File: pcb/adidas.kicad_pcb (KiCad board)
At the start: 2 copper layers, 152.7 x 107.2 mm, 34 parts, among them J1 ISP Header, J2 Shitty Add-on, J4 Battery, U1 MPU-6050, U2 ATTINY841-SSU

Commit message: RUN DRC
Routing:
- net GND: track 0.00 -> 367.1 mm, vias 0 -> 2
- net /7(SDA): track 0.00 -> 189.3 mm
- net /4(RST): track 0.00 -> 169.9 mm
- net /9(SCL): track 0.00 -> 167.8 mm, vias 0 -> 2
- net VCC: track 0.00 -> 149.7 mm
- net /3(LED Mid Row): track 0.00 -> 127.5 mm
- net Net-(D8-Pad2): track 0.00 -> 124.8 mm, vias 0 -> 1
- net Net-(J1-Pin_1): track 0.00 -> 121.6 mm, vias 0 -> 1
- net /2(LED Bottom Row): track 0.00 -> 101.6 mm
- net Net-(D4-Pad2): track 0.00 -> 100.2 mm, vias 0 -> 1
- net /13(SAO1): track 0.00 -> 92.9 mm, vias 0 -> 1
- net /12(SAO2): track 0.00 -> 90.5 mm, vias 0 -> 2
- net /5(LED Top Row): track 0.00 -> 88.3 mm, vias 0 -> 2
- net Net-(D1-Pad2): track 0.00 -> 71.6 mm, vias 0 -> 1
- net +BATT: track 0.00 -> 59.2 mm
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
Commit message: cleanup for v0.2
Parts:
- J4: value Battery -> мощность
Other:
- board text added: "THE @DEAD10C5 LOVE YOU!! @p0lr_ - Eddie the Yeti yaya_pancho - @thedevilsvoice"
- board text removed: "THE @DEAD10C5 LOVE YOU!! @p0lr_ - Eddie the Yeti yaya_pancho - @5l0w0n3 @thedevilsvoice"
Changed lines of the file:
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@@
         (effects (font (size 1 1) (thickness 0.15)) (justify mirror))
     )
-    (fp_text value "Battery" (at 0 -5.31) (layer "B.Fab")
+    (fp_text value "мощность" (at 0 -5.31) (layer "B.Fab")
         (effects (font (size 1 1) (thickness 0.15)) (justify mirror))
     )
@@
   (gr_line (start 100.93 110.14) (end 101.36 110.81)
     (stroke (width 0.1) (type solid)) (layer "Edge.Cuts"))
+  (gr_text "-" (at 150.9014 137.541) (layer "B.SilkS")
+    (effects (font (size 1.5 1.5) (thickness 0.3) bold) (justify left bottom mirror))
+  )
   (gr_text "SCK" (at 117.3226 100.0252 90) (layer "B.SilkS")
     (effects (font (size 0.8 0.8) (thickness 0.15)) (justify mirror))
@@
     (effects (font (size 0.6 0.6) (thickness 0.15)) (justify mirror))
   )
-  (gr_text "-" (at 106.7816 86.6394 180) (layer "B.SilkS")
-    (effects (font (size 0.6 0.6) (thickness 0.15)) (justify mirror))
-  )
   (gr_text "взаимоблокировщики - 31 октябрь 2022 г." (at 164.846 111.2012) (layer "B.SilkS")
     (effects (font (size 2 2) (thickness 0.3)) (justify mirror))
@@
     (effects (font (size 0.6 0.6) (thickness 0.15)) (justify mirror))
   )
-  (gr_text "THE @DEAD10C5 LOVE YOU!!\n@p0lr_ - Eddie the Yeti\nyaya_pancho - @5l0w0n3\n@thedevilsvoice " (at 228.6508 78.4352) (layer "B.SilkS")
+  (gr_text "THE @DEAD10C5 LOVE YOU!!\n@p0lr_ - Eddie the Yeti\nyaya_pancho - @thedevilsvoice " (at 228.6508 78.4352) (layer "B.SilkS")
     (effects (font (size 0.3 0.3) (thickness 0.075)) (justify mirror))
   )
@@
     (effects (font (size 2 2) (thickness 0.15)) (justify mirror))
   )
-  (gr_text "+" (at 101.4476 86.614 90) (layer "B.SilkS")
-    (effects (font (size 0.6 0.6) (thickness 0.15)) (justify mirror))
-  )
   (gr_text "Русский хардбасс" (at 165.1 123.0376) (layer "B.SilkS")
     (effects (font (size 3 3) (thickness 0.5)) (justify mirror))
@@
     (effects (font (size 0.8 0.8) (thickness 0.15)) (justify mirror))
   )
+  (gr_text "+" (at 150.9522 134.493) (layer "B.SilkS")
+    (effects (font (size 1.5 1.5) (thickness 0.3) bold) (justify left bottom mirror))
+  )
   (dimension (type aligned) (layer "B.Cu")

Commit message: final v0.2
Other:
- board text added: "SCL"
- board text added: "SDA"
- board text removed: "MISO"
- board text removed: "MOSI"
- board text removed: "SCK"

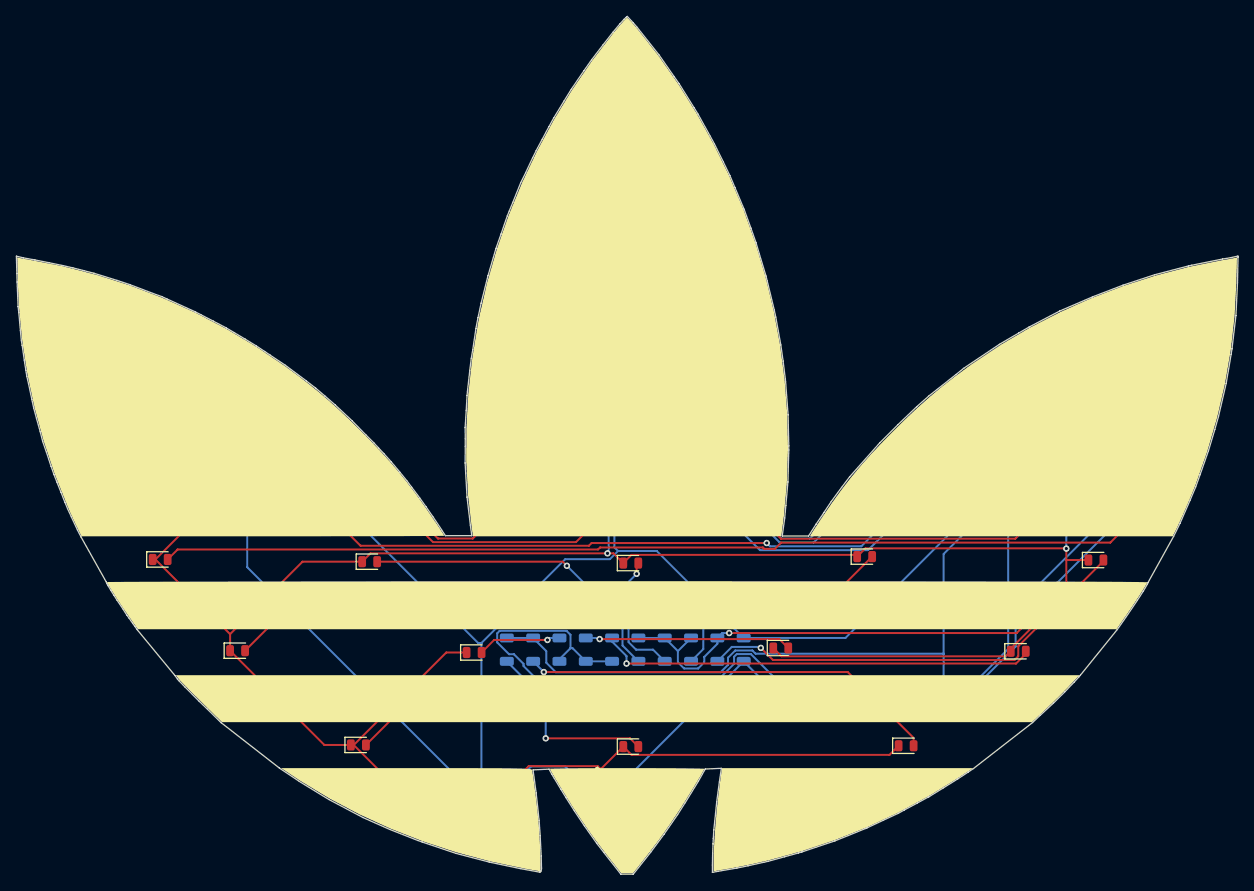
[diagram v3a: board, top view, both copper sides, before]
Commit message: make some changes from PCBway feedback v0.3 (#27)
* make some changes from PCBway feedback v0.3

* tune actions

* add mouser and digikey part numbers

* run ERC checks

* run ERC checks
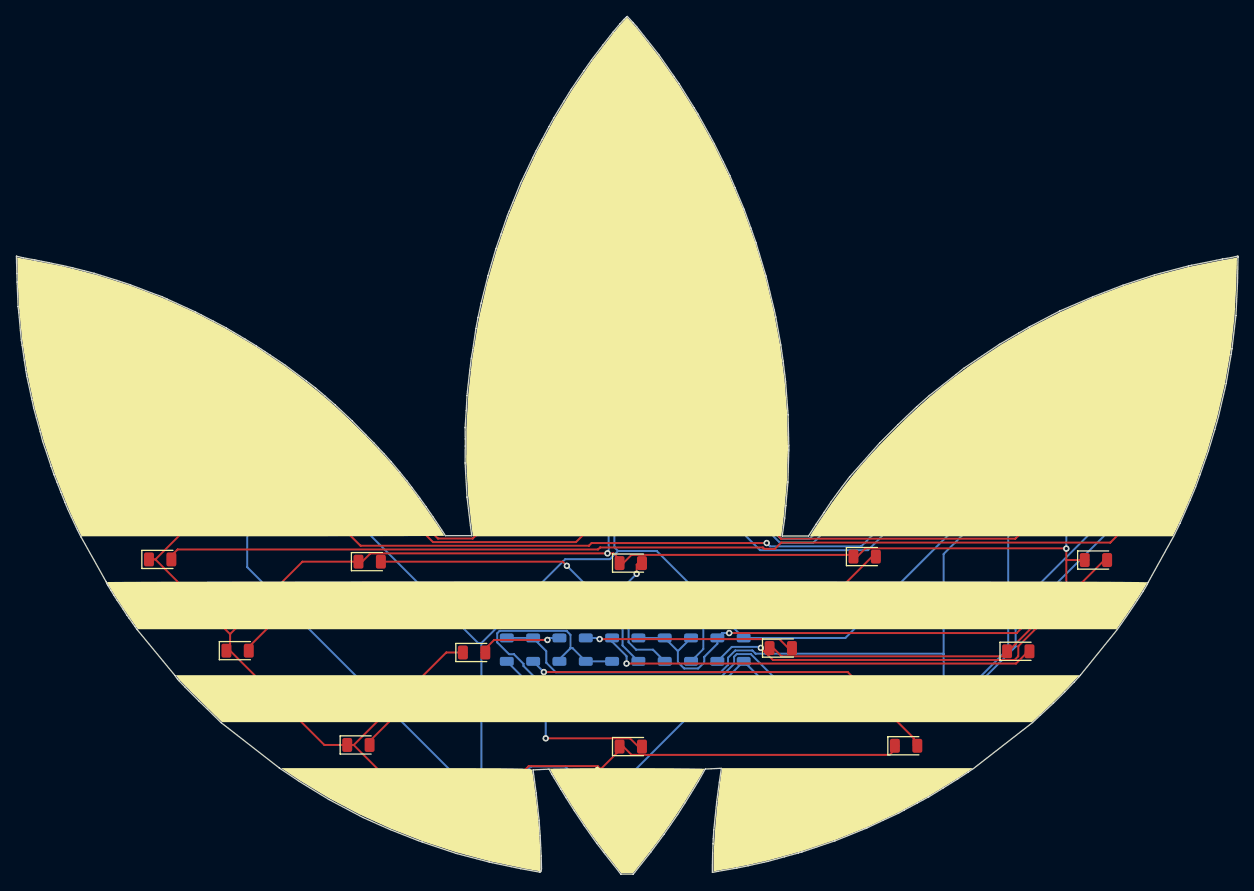
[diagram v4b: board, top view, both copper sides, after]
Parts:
- removed BT1: Battery_Cell, Battery:BatteryHolder_Keystone_3002_1x2032
- removed REF**: MountingHole_4.5mm, MountingHole:MountingHole_4.5mm
- D1, D10, D12, D2, D3, D4, D5, D6, D7, D8, D9: value LHN974 -> AP3216SYCK; footprint LED_SMD:LED_0805_2012Metric -> LED_SMD:LED_1206_3216Metric
- D11: value ~ -> AP3216SYCK; footprint LED_SMD:LED_0805_2012Metric -> LED_SMD:LED_1206_3216Metric
- J4: value мощность -> Battery
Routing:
- net +BATT: track 59.2 -> 0.00 mm
- net (no net): track 0.00 -> 59.2 mm

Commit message: BOM updates (#29)
* update schematic

* update schematic

* update the battery clip in the BOM
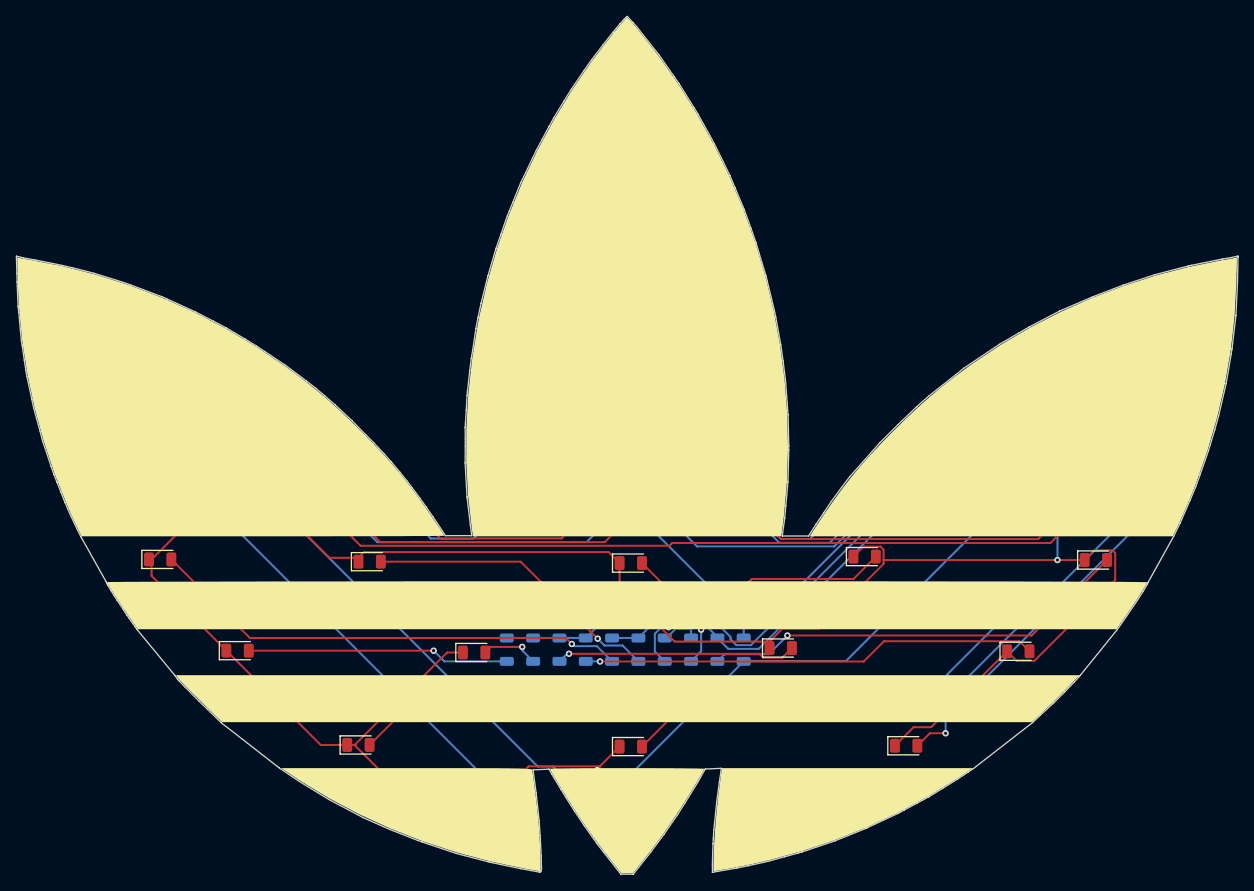
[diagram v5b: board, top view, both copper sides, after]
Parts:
- added BT1: Battery Clip, DEAD10C5:BatteryHolder_Keystone_3002_1x2032, B.Cu at (165.4, 82.8)
- D1, D10, D11, D12, D2, D3, D4, D5, D6, D7, D8, D9: value AP3216SYCK -> CTL1206FWH1T
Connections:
- J1 pad 2: VCC -> VDD
- J2 pad 1: VCC +3.3V -> VDD
- J4 pad 1: VCC -> VDD
- R13 pad 1: VCC -> VDD
- R2 pad 1: Net-(D4-Pad2) -> /2(LED Bottom Row)
- R2 pad 2: /3(LED Mid Row) -> Net-(D2-Pad2)
- R3 pad 1: /5(LED Top Row) -> /2(LED Bottom Row)
- R3 pad 2: Net-(D8-Pad2) -> Net-(D3-Pad2)
- R4 pad 1: /2(LED Bottom Row) -> /3(LED Mid Row)
- R4 pad 2: Net-(D2-Pad2) -> Net-(D4-Pad2)
- R5 pad 1: /2(LED Bottom Row) -> /3(LED Mid Row)
- R5 pad 2: Net-(D3-Pad2) -> Net-(D5-Pad2)
- R6 pad 1: Net-(D5-Pad2) -> /3(LED Mid Row)
- R6 pad 2: /3(LED Mid Row) -> Net-(D6-Pad2)
- R7 pad 1: Net-(D6-Pad2) -> /3(LED Mid Row)
- R7 pad 2: /3(LED Mid Row) -> Net-(D7-Pad2)
- R8 pad 1: Net-(D7-Pad2) -> /5(LED Top Row)
- R8 pad 2: /3(LED Mid Row) -> Net-(D8-Pad2)
- U1 pad 13: VCC -> VDD
- U2 pad 1: VCC -> VDD
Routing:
- net VDD: track 0.00 -> 225.6 mm
- net VCC: track 149.7 -> 0.00 mm
- net Net-(D4-Pad2): track 100.2 -> 32.8 mm
- net Net-(D8-Pad2): track 124.8 -> 60.4 mm
- net GND: track 367.1 -> 428.9 mm, vias 2 -> 1
- net (no net): track 59.2 -> 0.00 mm
- net /2(LED Bottom Row): track 101.6 -> 54.3 mm
- net /3(LED Mid Row): track 127.5 -> 87.6 mm
- net Net-(D2-Pad2): track 23.6 -> 53.6 mm
- net /7(SDA): track 189.3 -> 170.3 mm, vias 0 -> 2
- net /4(RST): track 169.9 -> 151.6 mm
- net Net-(D3-Pad2): track 52.5 -> 41.7 mm
- net /5(LED Top Row): track 88.3 -> 80.6 mm, vias 2 -> 0
- net Net-(J1-Pin_1): track 121.6 -> 113.9 mm
- net Net-(D6-Pad2): track 25.8 -> 30.2 mm
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
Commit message: update graphics (#31)
* update graphics

* change out the LED component
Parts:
- D1, D10, D11, D12, D2, D3, D4, D5, D6, D7, D8, D9: value CTL1206FWH1T -> SM1206NHC-IL

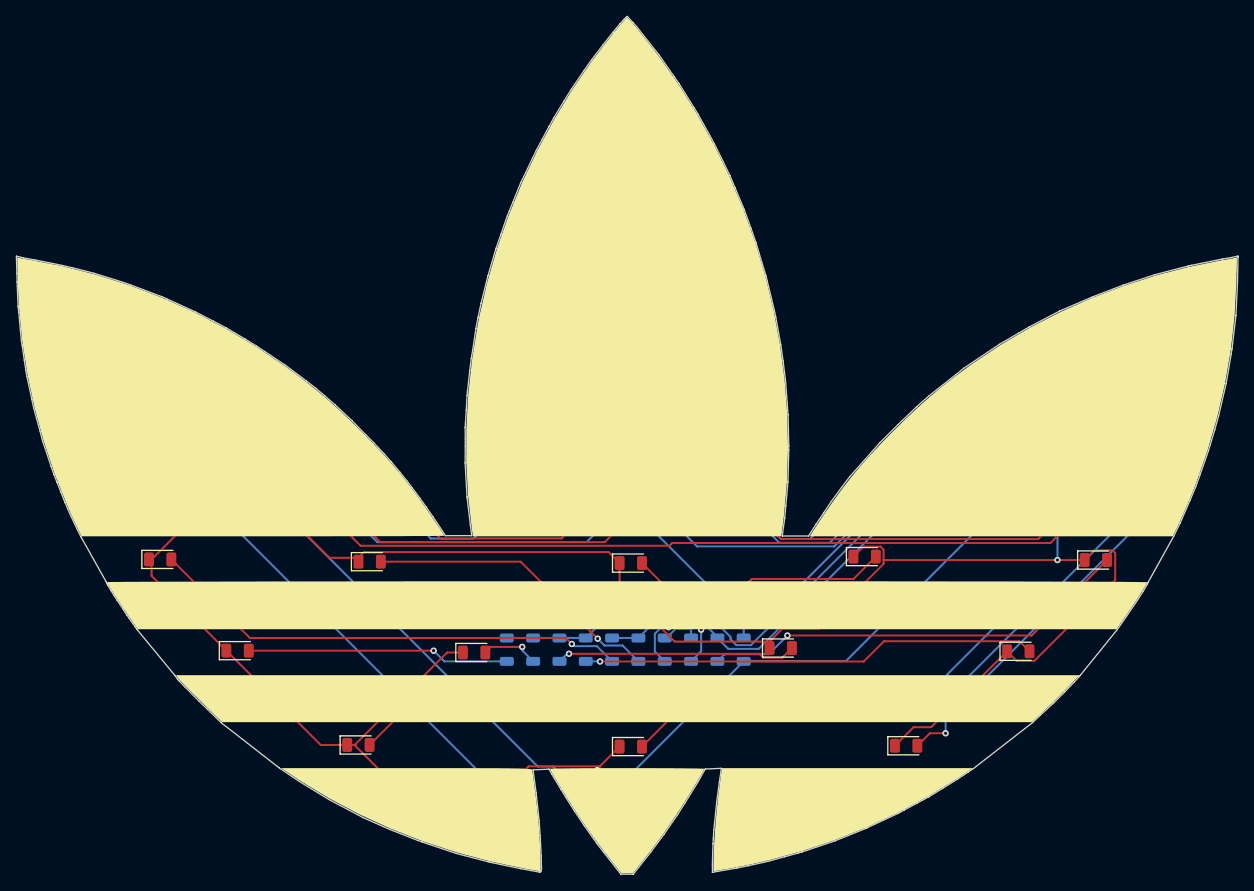
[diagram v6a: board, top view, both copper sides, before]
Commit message: replace B3F-100 switch (#40)
* replace B3F-100 switch

* update switches, re-add the lanyard hole
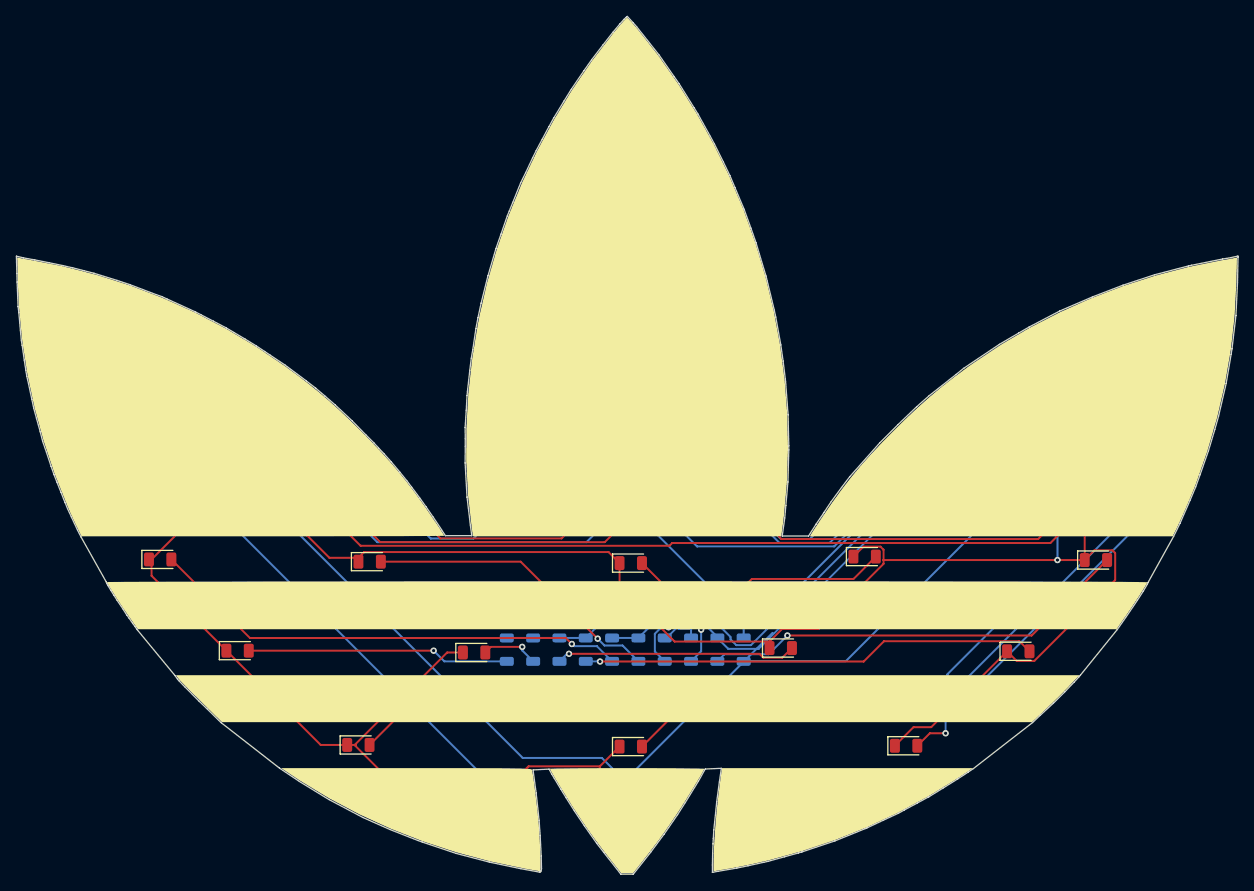
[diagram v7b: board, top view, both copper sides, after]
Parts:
- added R14: 470Ω, Resistor_SMD:R_1206_3216Metric, B.Cu at (224.0, 83.0)
- added REF**: MountingHole_4.5mm, DEAD10C5:MountingHole_4.5mm, F.Cu at (165.1, 48.5)
- added S2: TL1107BF180WQ, DEAD10C5:SW_TL1107BF130WQ, B.Cu at (234.2, 84.8)
- BT1: footprint DEAD10C5:BatteryHolder_Keystone_3002_1x2032 -> Resistor_SMD:R_1206_3216Metric
- S1: value B3F-1000 -> TL1107BF180WQ; footprint DEAD10C5:SW_B3F-1000 -> DEAD10C5:SW_TL1107BF130WQ; moved to B.Cu
- moved S1 1.27 mm to (164.8, 136.6), turned to -90 degrees
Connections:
- net /9(SCL) renamed /9(SCK)
- net Net-(J1-Pin_1) renamed /8(MOSI)
- S1 pad 1: GND -> /4(RST)
- S1 pad 2: unconnected-(S1-Pad2) -> GND
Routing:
- net /13(SAO1): track 93.0 -> 127.2 mm, vias 2 -> 3
- net GND: track 428.9 -> 461.1 mm
- net VDD: track 225.6 -> 235.7 mm, vias 0 -> 2
- net /4(RST): track 151.6 -> 152.5 mm
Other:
- board text added: ":: THE @DEAD10C5 LOVE YOU :: @p0lr_ Eddie the Yeti yaya_pancho @thedevilsvoice"
- board text added: "SCK"
- board text removed: "SCL"
- board text removed: "THE @DEAD10C5 LOVE YOU!! @p0lr_ - Eddie the Yeti yaya_pancho - @thedevilsvoice"

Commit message: remove all traces, move chip and battery holder
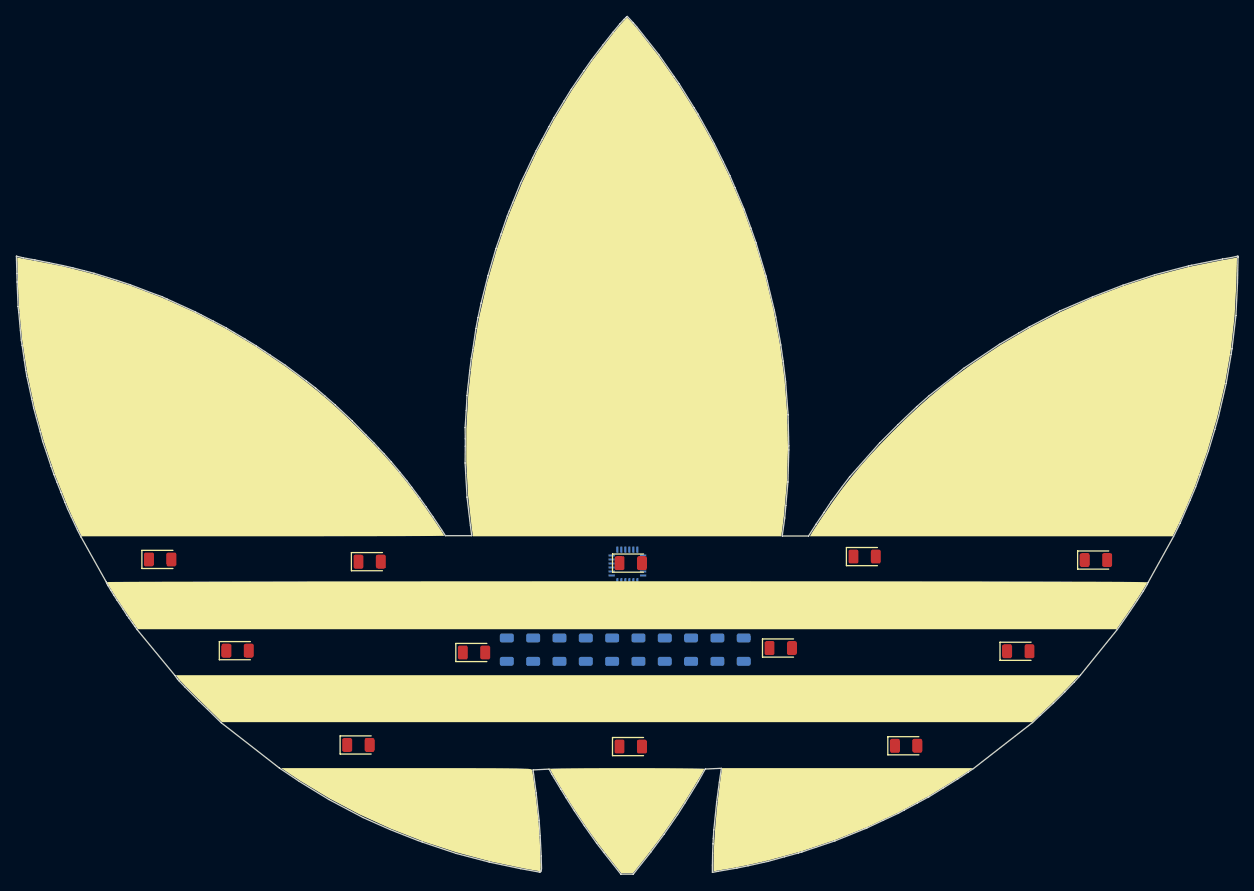
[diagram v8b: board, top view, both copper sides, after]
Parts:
- J2: moved to B.Cu
- moved BT1 11.2 mm to (165.7, 94.0)
- moved U1 7.21 mm to (165.1, 106.4)
- turned J2 to -90 degrees
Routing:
- net GND: track 461.1 -> 0.00 mm, vias 1 -> 0
- net VDD: track 235.7 -> 0.00 mm, vias 2 -> 0
- net /7(SDA): track 170.3 -> 0.00 mm, vias 2 -> 0
- net /9(SCK): track 164.1 -> 0.00 mm, vias 2 -> 0
- net /4(RST): track 152.5 -> 0.00 mm
- net /13(SAO1): track 127.2 -> 0.00 mm, vias 3 -> 0
- net /8(MOSI): track 113.9 -> 0.00 mm, vias 1 -> 0
- net /12(SAO2): track 91.1 -> 0.00 mm, vias 2 -> 0
- net /3(LED Mid Row): track 87.6 -> 0.00 mm
- net /5(LED Top Row): track 80.6 -> 0.00 mm
- net Net-(D1-Pad2): track 71.2 -> 0.00 mm, vias 1 -> 0
- net Net-(D8-Pad2): track 60.4 -> 0.00 mm, vias 1 -> 0
- net Net-(D7-Pad2): track 57.0 -> 0.00 mm, vias 1 -> 0
- net /2(LED Bottom Row): track 54.3 -> 0.00 mm
- net Net-(D12-Pad2): track 54.0 -> 0.00 mm, vias 1 -> 0
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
